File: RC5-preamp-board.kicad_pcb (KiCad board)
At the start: 2 copper layers, 76.2 x 41.3 mm, 32 parts, among them P1 RAW_DC, P10 CTL_OUT, P2 VCC, P201 FTDI Basic, P3 VCC, P4 VCC, P5 VCC, P6 VCC, P8 INPUTS, P9 UI_OUT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

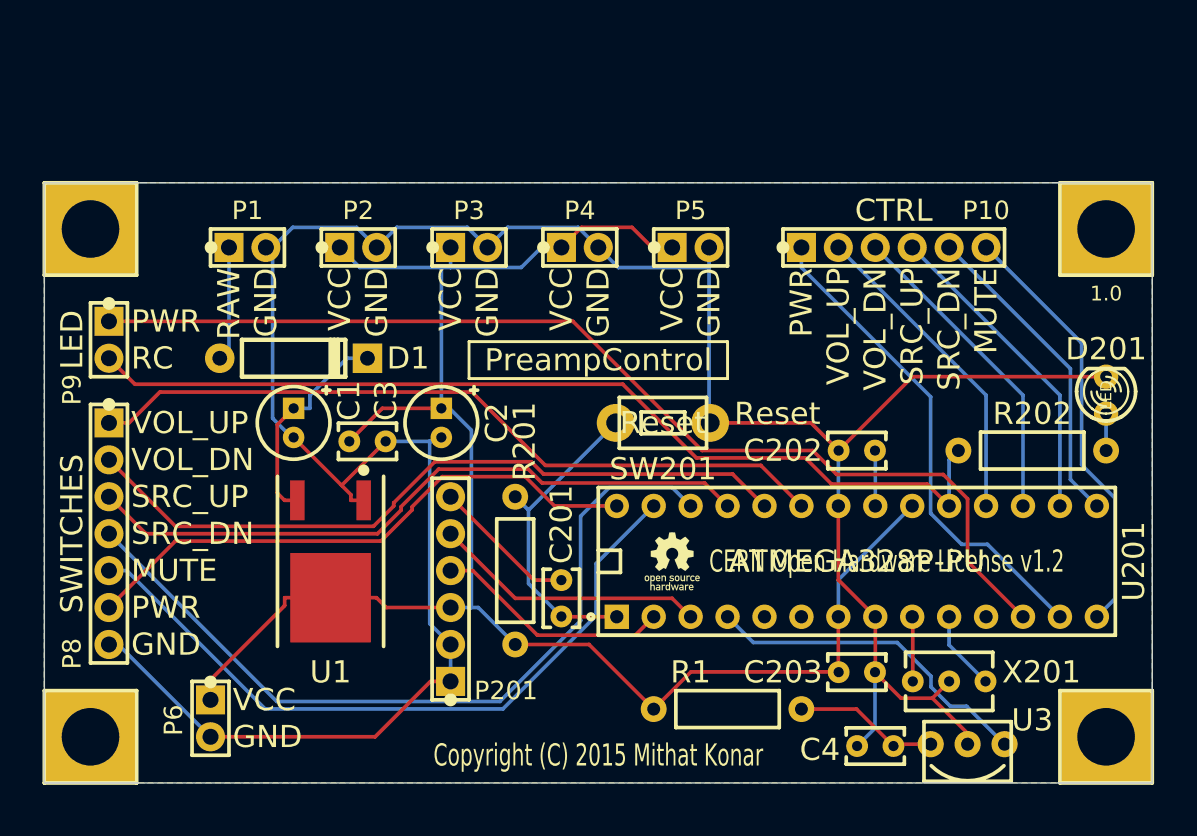
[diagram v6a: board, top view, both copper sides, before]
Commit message: Rerouted IR module output away from resonator.
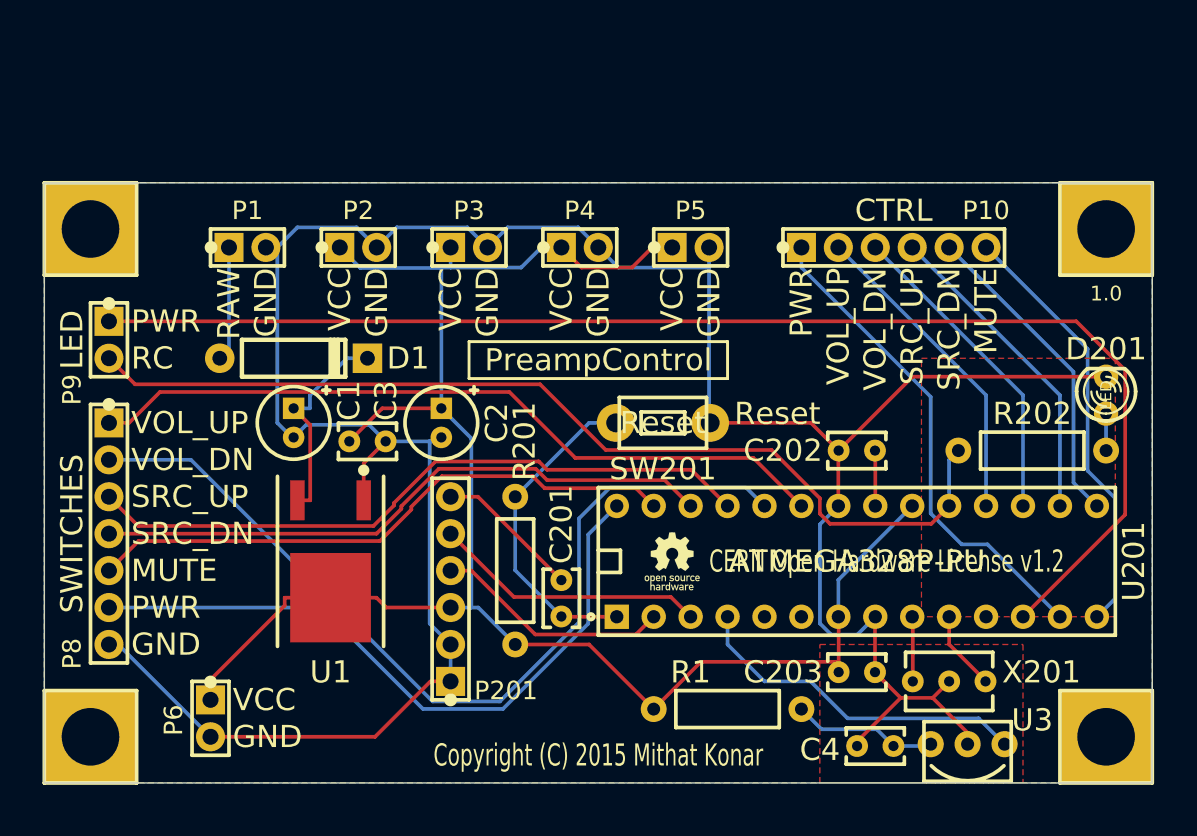
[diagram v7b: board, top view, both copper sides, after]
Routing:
- net /arduino-pcb/D6: track 73.8 -> 91.2 mm
- net /arduino-pcb/A3: track 55.6 -> 43.0 mm
- net /arduino-pcb/A1: track 50.2 -> 62.8 mm
- net /arduino-pcb/A4: track 49.3 -> 41.1 mm
- net /arduino-pcb/A5: track 39.6 -> 47.2 mm
- net DGND: track 182.7 -> 188.0 mm
- net /arduino-pcb/SCK: track 66.1 -> 67.7 mm
- net /arduino-pcb/D2: track 23.1 -> 23.8 mm
- net /arduino-pcb/RESET: track 21.8 -> 22.4 mm
- added copper zone on F.Cu, net DGND
